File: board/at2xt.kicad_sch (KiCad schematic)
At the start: 15 parts, among them J1 Conn_01x04, J2 XT, J3 AT, J4 PS/2, U1 MCP1700-3302E_TO92, U2 MSP430G2211IPW14

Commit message: Apply some suggestions from dragonmux's hoard.
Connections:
- net TCK: no longer names the net of J1.3 (Pin_3), U2.11 (SBWTCK/TEST)
- net TDIO: no longer names the net of C3.1, J1.1 (Pin_1), R1.2, U2.10 (~{RST}/NMI/SBWTDIO)
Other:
- note added: "GND"
- note added: "TCK"
- note added: "TDIO"
- note added: "VTGT"
- moved on the sheet: C3, J1, R1

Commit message: Annotate parts, regenerate PCB, gerbers, and drill file.
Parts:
- C1, C2: value 1u -> 2.2u; MFR (none) -> Kyocera AVX; MPN (none) -> 0603YD225KAT2A; OC_DIGIKEY (none) -> 478-5147-2-ND; OC_MOUSER (none) -> 581-0603YD225K; URL_DIGIKEY (none) -> https://www.digikey.com/en/products/detail/kyocera-avx/0603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; URL_MOUSER (none) -> https://www.mouser.com/ProductDetail/KYOCERA-AVX/0603YD225K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
- C3: MFR (none) -> Kyocera AVX; MPN (none) -> 0603YC102KAT2A; OC_DIGIKEY (none) -> 478-7933-2-ND; OC_MOUSER (none) -> 581-0603YC102KAT2A; URL_DIGIKEY (none) -> https://www.digikey.com/en/products/detail/kyocera-avx/0603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; URL_MOUSER (none) -> https://www.mouser.com/ProductDetail/KYOCERA-AVX/0603YC102K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
- C4: MFR (none) -> Kyocera AVX; MPN (none) -> 0603YC104KAT2A; OC_DIGIKEY (none) -> 478-1239-2-ND; OC_MOUSER (none) -> 581-06035C104JAT2A; URL_DIGIKEY (none) -> https://www.digikey.com/en/products/detail/kyocera-avx/0603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; URL_MOUSER (none) -> https://www.mouser.com/ProductDetail/KYOCERA-AVX/0603YC104K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
- J1: MFR (none) -> Samtec; MPN (none) -> TSW-104-14-S-S; OC_DIGIKEY (none) -> SAM1057-04-ND; OC_MOUSER (none) -> 200-TSW10414SS; URL_DIGIKEY (none) -> https://www.digikey.com/en/products/detail/samtec-inc/TSW-1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; URL_MOUSER (none) -> https://www.mouser.com/ProductDetail/Samtec/TSW-104-14-S-S?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
- J2, J3: MFR (none) -> Kycon; MPN (none) -> KCDX-5S-N; OC_DIGIKEY (none) -> 2092-KCDX-5S-N-ND; OC_MOUSER (none) -> 806-KCDX-5S-N; URL_DIGIKEY (none) -> https://www.digikey.com/en/products/detail/kycon-inc/KCDX-5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; URL_MOUSER (none) -> https://www.mouser.com/ProductDetail/Kycon/KCDX-5S-N?qs=uMQ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
- J4: MFR (none) -> Kycon; MPN (none) -> KMDGX-6S-N; OC_DIGIKEY (none) -> 2092-KMDGX-6S-BS-ND; OC_MOUSER (none) -> 806-KMDGX-6S-BS; URL_DIGIKEY (none) -> https://www.digikey.com/en/products/detail/kycon-inc/KMDGX-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; URL_MOUSER (none) -> https://www.mouser.com/ProductDetail/Kycon/KMDGX-6S-BS?qs=g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
- R1: MFR (none) -> Panasonic; MPN (none) -> ERJ-3GEYJ473V; OC_DIGIKEY (none) -> P47KGTR-ND; OC_MOUSER (none) -> 667-ERJ-3GEYJ473V; URL_DIGIKEY (none) -> https://www.digikey.com/en/products/detail/panasonic-electr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; URL_MOUSER (none) -> https://www.mouser.com/ProductDetail/Panasonic/ERJ-3GEYJ473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
- R2, R3, R4, R5: MFR (none) -> Panasonic; MPN (none) -> ERJ-3GEYJ301V; OC_DIGIKEY (none) -> P300GTR-ND; OC_MOUSER (none) -> 667-ERJ-3GEYJ301V; URL_DIGIKEY (none) -> https://www.digikey.com/en/products/detail/panasonic-electr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; URL_MOUSER (none) -> https://www.mouser.com/ProductDetail/Panasonic/ERJ-3GEYJ301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
- U1: value MCP1700-3302E_TO92 -> MCP1700x-330xxTT; MFR (none) -> Microchip; MPN (none) -> MCP1700T-3302E/TT; OC_DIGIKEY (none) -> MCP1700T3302ETTTR-ND; OC_MOUSER (none) -> 579-MCP1700T3302E/TT; URL_DIGIKEY (none) -> https://www.digikey.com/en/products/detail/microchip-techno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; URL_MOUSER (none) -> https://www.mouser.com/ProductDetail/Microchip-Technology-A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
- U2: MFR (none) -> Texas Instruments; MPN (none) -> MSP430G2211IPW14; OC_DIGIKEY (none) -> 296-25830-5-ND; OC_MOUSER (none) -> 595-MSP430G2211IPW14; URL_DIGIKEY (none) -> https://www.digikey.com/en/products/detail/texas-instrument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; URL_MOUSER (none) -> https://www.mouser.com/ProductDetail/Texas-Instruments/MSP4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

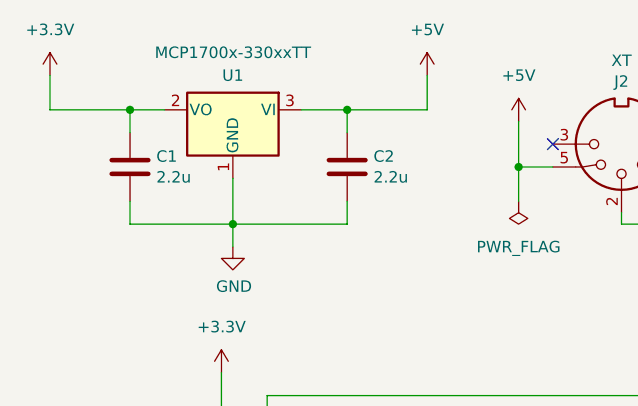
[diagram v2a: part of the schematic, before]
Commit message: Minor silkscreen fixups, swap out regulator for part readily available from Mouser.
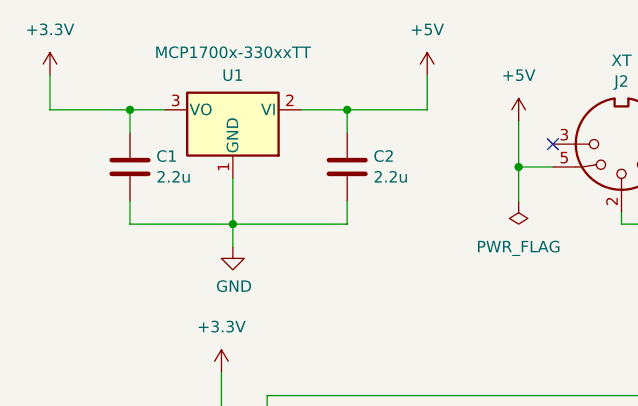
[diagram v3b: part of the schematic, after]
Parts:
- U1: footprint Package_TO_SOT_SMD:SOT-23 -> Package_TO_SOT_SMD:SOT-89-3; symbol Regulator_Linear:MCP1700x-330xxTT -> Regulator_Linear:MCP1700x-330xxMB; MPN MCP1700T-3302E/TT -> MCP1700T-3302E/MB; OC_DIGIKEY MCP1700T3302ETTTR-ND -> MCP1700T3302EMBTR-ND; OC_MOUSER 579-MCP1700T3302E/TT -> 579-MCP1700T3302E/MB; URL_DIGIKEY https://www.digikey.com/en/products/detail/microchip-technology/MCP1700T-3302E-TT/652676 -> https://www.digikey.com/en/products/detail/microchip-technology/MCP1700T-3302E-MB/652678; URL_MOUSER https://www.mouser.com/ProductDetail/Microchip-Technology-Atmel/MCP1700T-3302E-TT?qs=fM4xO01eazPmCNDrdHEdaw%3D%3D -> https://www.mouser.com/ProductDetail/Microchip-Technology-Atmel/MCP1700T-3302E-MB?qs=WWgnj3qycfnlJJhwyn%2Fifw%3D%3D
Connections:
- net +3.3V: now also U1.3 (VO); no longer U1.2 (VO)
- net +5V: now also U1.2 (VI); no longer U1.3 (VI)
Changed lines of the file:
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@@
     (pin "1")
   )
-  (symbol (lib_id "Regulator_Linear:MCP1700x-330xxTT") (at 76.2 43.18 0) (mirror y) (unit 1)
+  (symbol (lib_id "Regulator_Linear:MCP1700x-330xxMB") (at 76.2 43.18 0) (mirror y) (unit 1)
     (in_bom yes) (on_board yes)
     (property "Reference" "U1" (id 0) (at 76.2 39.37 0))
     (property "Value" "MCP1700x-330xxTT" (id 1) (at 76.2 36.83 0))
-    (property "Footprint" "Package_TO_SOT_SMD:SOT-23" (id 2) (at 76.2 37.465 0)
-      (effects (font (size 1.27 1.27)) hide)
-    )
-    (property "Datasheet" "https://ww1.microchip.com/downloads/aemDocuments/documents/APID/ProductDocuments/DataSheets/MCP1700-Data-Sheet-20001826F.pdf" (id 3) (at 76.2 43.18 0)
+    (property "Footprint" "Package_TO_SOT_SMD:SOT-89-3" (id 2) (at 76.2 38.1 0)
+      (effects (font (size 1.27 1.27)) hide)
+    )
+    (property "Datasheet" "http://ww1.microchip.com/downloads/en/DeviceDoc/20001826D.pdf" (id 3) (at 76.2 44.45 0)
       (effects (font (size 1.27 1.27)) hide)
     )
@@
       (effects (font (size 1.27 1.27)) hide)
     )
-    (property "MPN" "MCP1700T-3302E/TT" (id 5) (at 76.2 43.18 0)
-      (effects (font (size 1.27 1.27)) hide)
-    )
-    (property "OC_DIGIKEY" "MCP1700T3302ETTTR-ND" (id 6) (at 76.2 43.18 0)
-      (effects (font (size 1.27 1.27)) hide)
-    )
-    (property "OC_MOUSER" " 579-MCP1700T3302E/TT" (id 7) (at 76.2 43.18 0)
-      (effects (font (size 1.27 1.27)) hide)
-    )
-    (property "URL_DIGIKEY" "https://www.digikey.com/en/products/detail/microchip-technology/MCP1700T-3302E-TT/652676" (id 8) (at 76.2 43.18 0)
-      (effects (font (size 1.27 1.27)) hide)
-    )
-    (property "URL_MOUSER" "https://www.mouser.com/ProductDetail/Microchip-Technology-Atmel/MCP1700T-3302E-TT?qs=fM4xO01eazPmCNDrdHEdaw%3D%3D" (id 9) (at 76.2 43.18 0)
+    (property "MPN" "MCP1700T-3302E/MB" (id 5) (at 76.2 43.18 0)
+      (effects (font (size 1.27 1.27)) hide)
+    )
+    (property "OC_DIGIKEY" "MCP1700T3302EMBTR-ND" (id 6) (at 76.2 43.18 0)
+      (effects (font (size 1.27 1.27)) hide)
+    )
+    (property "OC_MOUSER" "579-MCP1700T3302E/MB" (id 7) (at 76.2 43.18 0)
+      (effects (font (size 1.27 1.27)) hide)
+    )
+    (property "URL_DIGIKEY" "https://www.digikey.com/en/products/detail/microchip-technology/MCP1700T-3302E-MB/652678" (id 8) (at 76.2 43.18 0)
+      (effects (font (size 1.27 1.27)) hide)
+    )
+    (property "URL_MOUSER" "https://www.mouser.com/ProductDetail/Microchip-Technology-Atmel/MCP1700T-3302E-MB?qs=WWgnj3qycfnlJJhwyn%2Fifw%3D%3D" (id 9) (at 76.2 43.18 0)
       (effects (font (size 1.27 1.27)) hide)
     )
@@
     )
     (path "/00000000-0000-0000-0000-00005b0cfc32"
-      (reference "U1") (unit 1) (value "MCP1700x-330xxTT") (footprint "Package_TO_SOT_SMD:SOT-23")
+      (reference "U1") (unit 1) (value "MCP1700x-330xxTT") (footprint "Package_TO_SOT_SMD:SOT-89-3")
     )
     (path "/00000000-0000-0000-0000-00005b0bd296"

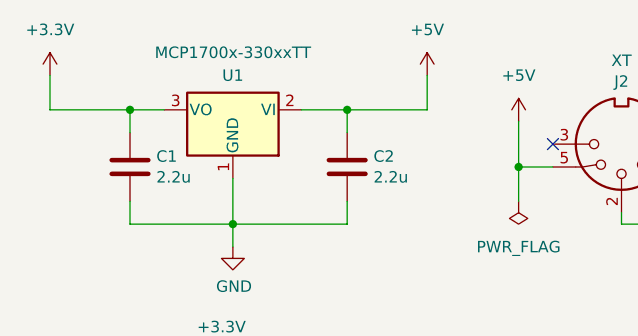
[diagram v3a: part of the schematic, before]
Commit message: Fix errant value for regulator (wrong identifier, correct package).
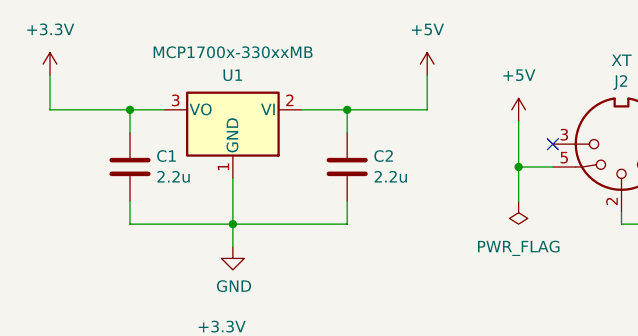
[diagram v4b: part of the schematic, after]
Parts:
- U1: value MCP1700x-330xxTT -> MCP1700x-330xxMB
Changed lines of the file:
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@@
     (in_bom yes) (on_board yes)
     (property "Reference" "U1" (id 0) (at 76.2 39.37 0))
-    (property "Value" "MCP1700x-330xxTT" (id 1) (at 76.2 36.83 0))
+    (property "Value" "MCP1700x-330xxMB" (id 1) (at 76.2 36.83 0))
     (property "Footprint" "Package_TO_SOT_SMD:SOT-89-3" (id 2) (at 76.2 38.1 0)
       (effects (font (size 1.27 1.27)) hide)
@@
     )
     (path "/00000000-0000-0000-0000-00005b0cfc32"
-      (reference "U1") (unit 1) (value "MCP1700x-330xxTT") (footprint "Package_TO_SOT_SMD:SOT-89-3")
+      (reference "U1") (unit 1) (value "MCP1700x-330xxMB") (footprint "Package_TO_SOT_SMD:SOT-89-3")
     )
     (path "/00000000-0000-0000-0000-00005b0bd296"

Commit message: Fixed OC_MOUSER for one of the capacitors.
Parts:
- C4: OC_MOUSER 581-06035C104JAT2A -> 581-06035C104KAT2A
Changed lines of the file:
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@@
       (effects (font (size 1.27 1.27)) hide)
     )
-    (property "OC_MOUSER" "581-06035C104JAT2A" (id 7) (at 105.41 96.52 0)
+    (property "OC_MOUSER" "581-06035C104KAT2A" (id 7) (at 105.41 96.52 0)
       (effects (font (size 1.27 1.27)) hide)
     )

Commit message: More BOM fixes. NFC.
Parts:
- C3: MPN 0603YC102KAT2A -> 06033C112KAT2A; OC_DIGIKEY 478-7933-2-ND -> 06033C112KAT2A-ND; OC_MOUSER 581-0603YC102KAT2A -> 581-06033C112KAT2A; URL_DIGIKEY https://www.digikey.com/en/products/detail/kyocera-avx/0603YC104KAT2A/563349 -> https://www.digikey.com/en/products/detail/kyocera-avx/06033C112KAT2A/1599375; URL_MOUSER https://www.mouser.com/ProductDetail/KYOCERA-AVX/0603YC102K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 -> https://www.mouser.com/ProductDetail/KYOCERA-AVX/06033C112K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
- C4: URL_DIGIKEY https://www.digikey.com/en/products/detail/kyocera-avx/0603YC102KAT2A/1600482 -> https://www.digikey.com/en/products/detail/kyocera-avx/0603YC104KAT2A/563349
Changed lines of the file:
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@@
       (effects (font (size 1.27 1.27)) hide)
     )
-    (property "MPN" "0603YC102KAT2A" (id 5) (at 83.82 96.52 0)
+    (property "MPN" "06033C112KAT2A" (id 5) (at 83.82 96.52 0)
       (effects (font (size 1.27 1.27)) hide)
     )
-    (property "OC_DIGIKEY" "478-7933-2-ND" (id 6) (at 83.82 96.52 0)
+    (property "OC_DIGIKEY" "06033C112KAT2A-ND" (id 6) (at 83.82 96.52 0)
       (effects (font (size 1.27 1.27)) hide)
     )
-    (property "OC_MOUSER" "581-0603YC102KAT2A" (id 7) (at 83.82 96.52 0)
+    (property "OC_MOUSER" "581-06033C112KAT2A" (id 7) (at 83.82 96.52 0)
       (effects (font (size 1.27 1.27)) hide)
     )
-    (property "URL_DIGIKEY" "https://www.digikey.com/en/products/detail/kyocera-avx/0603YC104KAT2A/563349" (id 8) (at 83.82 96.52 0)
+    (property "URL_DIGIKEY" "https://www.digikey.com/en/products/detail/kyocera-avx/06033C112KAT2A/1599375" (id 8) (at 83.82 96.52 0)
       (effects (font (size 1.27 1.27)) hide)
     )
-    (property "URL_MOUSER" "https://www.mouser.com/ProductDetail/KYOCERA-AVX/0603YC102KAT2A?qs=J0cf14owUtQZ3o2WGChX2A%3D%3D" (id 9) (at 83.82 96.52 0)
+    (property "URL_MOUSER" "https://www.mouser.com/ProductDetail/KYOCERA-AVX/06033C112KAT2A?qs=EbDiPP9peV8hs81P1YU3Ig%3D%3D" (id 9) (at 83.82 96.52 0)
       (effects (font (size 1.27 1.27)) hide)
     )
@@
       (effects (font (size 1.27 1.27)) hide)
     )
-    (property "URL_DIGIKEY" "https://www.digikey.com/en/products/detail/kyocera-avx/0603YC102KAT2A/1600482" (id 8) (at 105.41 96.52 0)
+    (property "URL_DIGIKEY" "https://www.digikey.com/en/products/detail/kyocera-avx/0603YC104KAT2A/563349" (id 8) (at 105.41 96.52 0)
       (effects (font (size 1.27 1.27)) hide)
     )
